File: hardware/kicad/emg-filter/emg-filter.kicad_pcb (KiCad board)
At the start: 4 copper layers, 113.7 x 234.3 mm, 78 parts, among them J1 Conn_01x02, J10 Conn_01x02, J11 Conn_01x05, J12 Conn_01x02, J13 Conn_01x02, J14 Conn_01x05, J15 Conn_01x02, J16 Conn_01x02, J17 Conn_01x05, J18 Conn_01x02, J19 Conn_01x02, J2 Conn_01x03, J20 Conn_01x05, J21 Conn_01x02, J22 Conn_01x02, J23 Conn_01x05, J24 Conn_01x02, J25 Conn_01x02, J26 Conn_01x05, J27 Conn_01x02, J28 Conn_01x02, J29 Conn_01x02, J3 Conn_02x20_Odd_Even, J30 Conn_01x02, J31 Conn_01x02, J32 Conn_01x02, J33 Conn_01x02, J34 Conn_01x02, J35 Conn_01x02, J36 Conn_01x02, J37 Conn_01x02, J38 Conn_01x02, J39 Conn_01x02, J4 Conn_01x02, J40 Conn_01x02, J41 Conn_01x02, J5 Conn_01x05, J6 Conn_01x02, J7 Conn_01x02, J8 Conn_01x05, J9 Conn_01x02, U1 LM7805_TO220, U2 LM7905_TO220, U3 ADC108S102, U4 ADC108S102

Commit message: saving progress
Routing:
- net !CS_2_PI: track 142.1 -> 135.9 mm, vias 3 -> 2
- net +3V3: track 193.7 -> 190.8 mm, vias 4 -> 3
- net SCLK_CLK_PI: track 188.6 -> 187.0 mm
- net DIN_MOSI_PI: track 191.0 -> 190.1 mm, vias 4 -> 3
- net AGND: vias 87 -> 97
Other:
- board text added: "1"
- board text added: "2"
- board text added: "3"
- board text added: "4"
- board text added: "5"
- board text added: "6"
- board text added: "7"
- board text added: "8"

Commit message: saving progress
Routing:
- net AGND: vias 97 -> 92

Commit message: gerbers
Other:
- board text added: "Prosthetic Limb EMG Motherboard Concordia University Capstone 2022 KNVBMZSFSSHS"
- board text removed: "Prosthetic Limb EMG Motherboard Concordia University Capstone 2022 VBKNMZSFSSHS"
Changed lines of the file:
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@@
     (thickness 1.6)
     (drawings 95)
-    (tracks 515)
+    (tracks 513)
     (zones 0)
     (modules 78)
@@
     (visible_elements 7FFFFFFF)
     (pcbplotparams
-      (layerselection 0x010fc_ffffffff)
+      (layerselection 0x010f0_ffffffff)
       (usegerberextensions false)
       (usegerberattributes true)
@@
       (linewidth 0.100000)
       (plotframeref false)
-      (viasonmask false)
+      (viasonmask true)
       (mode 1)
       (useauxorigin false)
@@
       (outputformat 1)
       (mirror false)
-      (drillshape 1)
+      (drillshape 0)
       (scaleselection 1)
-      (outputdirectory ""))
+      (outputdirectory "gerber/"))
   )
   (net 0 "")
@@
       (effects (font (size 0.5 0.5) (thickness 0.08)))
     )
-    (pad 1 smd roundrect (at -0.9125 0 270) (size 1.025 1.4) (layers F.Cu F.Paste F.Mask) (roundrect_rratio 0.243902)
+    (pad 1 smd roundrect (at -0.9125 0 270) (size 1.025 1.4) (layers F.Cu F.Paste F.Mask) (roundrect_rratio 0.2439014634146341)
       (net 8 "Net-(D3-Pad1)"))
-    (pad 2 smd roundrect (at 0.9125 0 270) (size 1.025 1.4) (layers F.Cu F.Paste F.Mask) (roundrect_rratio 0.243902)
+    (pad 2 smd roundrect (at 0.9125 0 270) (size 1.025 1.4) (layers F.Cu F.Paste F.Mask) (roundrect_rratio 0.2439014634146341)
       (net 5 -5V))
     (model ${KISYS3DMOD}/Resistor_SMD.3dshapes/R_0805_2012Metric.wrl
@@
       (effects (font (size 0.5 0.5) (thickness 0.08)))
     )
-    (pad 2 smd roundrect (at 0.9125 0 180) (size 1.025 1.4) (layers F.Cu F.Paste F.Mask) (roundrect_rratio 0.243902)
+    (pad 2 smd roundrect (at 0.9125 0 180) (size 1.025 1.4) (layers F.Cu F.Paste F.Mask) (roundrect_rratio 0.2439014634146341)
       (net 5 -5V))
-    (pad 1 smd roundrect (at -0.9125 0 180) (size 1.025 1.4) (layers F.Cu F.Paste F.Mask) (roundrect_rratio 0.243902)
+    (pad 1 smd roundrect (at -0.9125 0 180) (size 1.025 1.4) (layers F.Cu F.Paste F.Mask) (roundrect_rratio 0.2439014634146341)
       (net 15 "Net-(R5-Pad2)"))
     (model ${KISYS3DMOD}/Resistor_SMD.3dshapes/R_0805_2012Metric.wrl
@@
       (effects (font (size 0.5 0.5) (thickness 0.08)))
     )
-    (pad 1 smd roundrect (at -0.9125 0 180) (size 1.025 1.4) (layers F.Cu F.Paste F.Mask) (roundrect_rratio 0.243902)
+    (pad 1 smd roundrect (at -0.9125 0 180) (size 1.025 1.4) (layers F.Cu F.Paste F.Mask) (roundrect_rratio 0.2439014634146341)
       (net 2 AGND))
-    (pad 2 smd roundrect (at 0.9125 0 180) (size 1.025 1.4) (layers F.Cu F.Paste F.Mask) (roundrect_rratio 0.243902)
+    (pad 2 smd roundrect (at 0.9125 0 180) (size 1.025 1.4) (layers F.Cu F.Paste F.Mask) (roundrect_rratio 0.2439014634146341)
       (net 15 "Net-(R5-Pad2)"))
     (model ${KISYS3DMOD}/Resistor_SMD.3dshapes/R_0805_2012Metric.wrl
@@
       (effects (font (size 0.5 0.5) (thickness 0.08)))
     )
-    (pad 1 smd roundrect (at -0.9125 0 270) (size 1.025 1.4) (layers F.Cu F.Paste F.Mask) (roundrect_rratio 0.243902)
+    (pad 1 smd roundrect (at -0.9125 0 270) (size 1.025 1.4) (layers F.Cu F.Paste F.Mask) (roundrect_rratio 0.2439014634146341)
       (net 2 AGND))
-    (pad 2 smd roundrect (at 0.9125 0 270) (size 1.025 1.4) (layers F.Cu F.Paste F.Mask) (roundrect_rratio 0.243902)
+    (pad 2 smd roundrect (at 0.9125 0 270) (size 1.025 1.4) (layers F.Cu F.Paste F.Mask) (roundrect_rratio 0.2439014634146341)
       (net 4 GNDREF))
     (model ${KISYS3DMOD}/Resistor_SMD.3dshapes/R_0805_2012Metric.wrl
@@
       (effects (font (size 0.5 0.5) (thickness 0.08)))
     )
-    (pad 1 smd roundrect (at -0.9125 0 270) (size 1.025 1.4) (layers F.Cu F.Paste F.Mask) (roundrect_rratio 0.243902)
+    (pad 1 smd roundrect (at -0.9125 0 270) (size 1.025 1.4) (layers F.Cu F.Paste F.Mask) (roundrect_rratio 0.2439014634146341)
       (net 7 "Net-(D2-Pad1)"))
-    (pad 2 smd roundrect (at 0.9125 0 270) (size 1.025 1.4) (layers F.Cu F.Paste F.Mask) (roundrect_rratio 0.243902)
+    (pad 2 smd roundrect (at 0.9125 0 270) (size 1.025 1.4) (layers F.Cu F.Paste F.Mask) (roundrect_rratio 0.2439014634146341)
       (net 2 AGND))
     (model ${KISYS3DMOD}/Resistor_SMD.3dshapes/R_0805_2012Metric.wrl
@@
       (effects (font (size 0.5 0.5) (thickness 0.08)))
     )
-    (pad 1 smd roundrect (at -0.9125 0 270) (size 1.025 1.4) (layers F.Cu F.Paste F.Mask) (roundrect_rratio 0.243902)
+    (pad 1 smd roundrect (at -0.9125 0 270) (size 1.025 1.4) (layers F.Cu F.Paste F.Mask) (roundrect_rratio 0.2439014634146341)
       (net 1 +24V))
-    (pad 2 smd roundrect (at 0.9125 0 270) (size 1.025 1.4) (layers F.Cu F.Paste F.Mask) (roundrect_rratio 0.243902)
+    (pad 2 smd roundrect (at 0.9125 0 270) (size 1.025 1.4) (layers F.Cu F.Paste F.Mask) (roundrect_rratio 0.2439014634146341)
       (net 2 AGND))
     (model ${KISYS3DMOD}/Resistor_SMD.3dshapes/R_0805_2012Metric.wrl
@@
       (effects (font (size 0.5 0.5) (thickness 0.08)))
     )
-    (pad 1 smd roundrect (at -0.9125 0 90) (size 1.025 1.4) (layers F.Cu F.Paste F.Mask) (roundrect_rratio 0.243902)
+    (pad 1 smd roundrect (at -0.9125 0 90) (size 1.025 1.4) (layers F.Cu F.Paste F.Mask) (roundrect_rratio 0.2439014634146341)
       (net 3 +5V))
-    (pad 2 smd roundrect (at 0.9125 0 90) (size 1.025 1.4) (layers F.Cu F.Paste F.Mask) (roundrect_rratio 0.243902)
+    (pad 2 smd roundrect (at 0.9125 0 90) (size 1.025 1.4) (layers F.Cu F.Paste F.Mask) (roundrect_rratio 0.2439014634146341)
       (net 14 "Net-(R1-Pad2)"))
     (model ${KISYS3DMOD}/Resistor_SMD.3dshapes/R_0805_2012Metric.wrl
@@
     (effects (font (size 1 1) (thickness 0.15)))
   )
-  (gr_text "Prosthetic Limb EMG Motherboard\nConcordia University Capstone 2022\nVBKNMZSFSSHS" (at 72.39 189.23) (layer F.SilkS)
+  (gr_text "Prosthetic Limb EMG Motherboard\nConcordia University Capstone 2022\nKNVBMZSFSSHS" (at 72.39 189.23) (layer F.SilkS)
     (effects (font (size 1 1) (thickness 0.15)))
   )
@@
   (via (at 108.204 196.85) (size 0.8) (drill 0.4) (layers F.Cu B.Cu) (net 2))
   (via (at 118.364 196.85) (size 0.8) (drill 0.4) (layers F.Cu B.Cu) (net 2))
-  (segment (start 69.9008 101.0412) (end 69.2658 101.0412) (width 0.25) (layer F.Cu) (net 2))
-  (segment (start 70.243535 100.698465) (end 69.9008 101.0412) (width 0.25) (layer F.Cu) (net 2))
-  (segment (start 70.931506 100.698465) (end 70.243535 100.698465) (width 0.25) (layer F.Cu) (net 2))
+  (segment (start 69.608535 100.698465) (end 69.2658 101.0412) (width 0.25) (layer F.Cu) (net 2))
+  (segment (start 70.931506 100.698465) (end 69.608535 100.698465) (width 0.25) (layer F.Cu) (net 2))
   (segment (start 71.116041 100.883) (end 70.931506 100.698465) (width 0.25) (layer F.Cu) (net 2))
   (segment (start 72.8215 100.883) (end 71.116041 100.883) (width 0.25) (layer F.Cu) (net 2))
@@
   (segment (start 82.777049 97.028) (end 114.554 97.028) (width 0.25) (layer B.Cu) (net 6))
   (segment (start 82.742264 96.993215) (end 82.777049 97.028) (width 0.25) (layer B.Cu) (net 6))
-  (segment (start 152.908 97.028) (end 114.427 97.028) (width 0.25) (layer B.Cu) (net 6))
+  (segment (start 152.908 97.028) (end 114.554 97.028) (width 0.25) (layer B.Cu) (net 6))
   (segment (start 141.224 -12.2705) (end 141.4295 -12.2705) (width 0.25) (layer F.Cu) (net 7))
   (segment (start 141.4295 -12.2705) (end 142.24 -13.081) (width 0.25) (layer F.Cu) (net 7))
@@
   (via (at 112.014 95.504) (size 0.8) (drill 0.4) (layers F.Cu B.Cu) (net 11))
   (segment (start 112.014 199.39) (end 112.014 95.504) (width 0.25) (layer F.Cu) (net 11))
-  (segment (start 81.534 95.504) (end 151.638 95.504) (width 0.25) (layer B.Cu) (net 11))
+  (segment (start 81.534 95.504) (end 112.014 95.504) (width 0.25) (layer B.Cu) (net 11))
+  (segment (start 112.014 95.504) (end 151.638 95.504) (width 0.25) (layer B.Cu) (net 11))
   (segment (start 78.5465 100.233) (end 79.599 100.233) (width 0.25) (layer F.Cu) (net 12))
   (via (at 80.01 94.742) (size 0.8) (drill 0.4) (layers F.Cu B.Cu) (net 12))
@@
   (segment (start 148.6585 100.229) (end 149.707 100.229) (width 0.25) (layer F.Cu) (net 12))
   (via (at 150.114004 94.742) (size 0.8) (drill 0.4) (layers F.Cu B.Cu) (net 12))
-  (segment (start 110.744 94.742) (end 110.74866 94.73734) (width 0.25) (layer B.Cu) (net 12))
-  (segment (start 80.01 94.742) (end 110.744 94.742) (width 0.25) (layer B.Cu) (net 12))
-  (segment (start 110.75332 94.742) (end 110.74866 94.73734) (width 0.25) (layer B.Cu) (net 12))
-  (segment (start 150.114004 94.742) (end 110.75332 94.742) (width 0.25) (layer B.Cu) (net 12))
   (via (at 109.474 94.742) (size 0.8) (drill 0.4) (layers F.Cu B.Cu) (net 12))
   (segment (start 109.474 199.39) (end 109.474 94.742) (width 0.25) (layer F.Cu) (net 12))
+  (segment (start 109.474 94.742) (end 150.114004 94.742) (width 0.25) (layer B.Cu) (net 12))
+  (segment (start 109.474 94.742) (end 80.01 94.742) (width 0.25) (layer B.Cu) (net 12))
   (via (at 148.59 93.853) (size 0.8) (drill 0.4) (layers F.Cu B.Cu) (net 13))
   (segment (start 148.59 99.5105) (end 148.6585 99.579) (width 0.25) (layer F.Cu) (net 13))

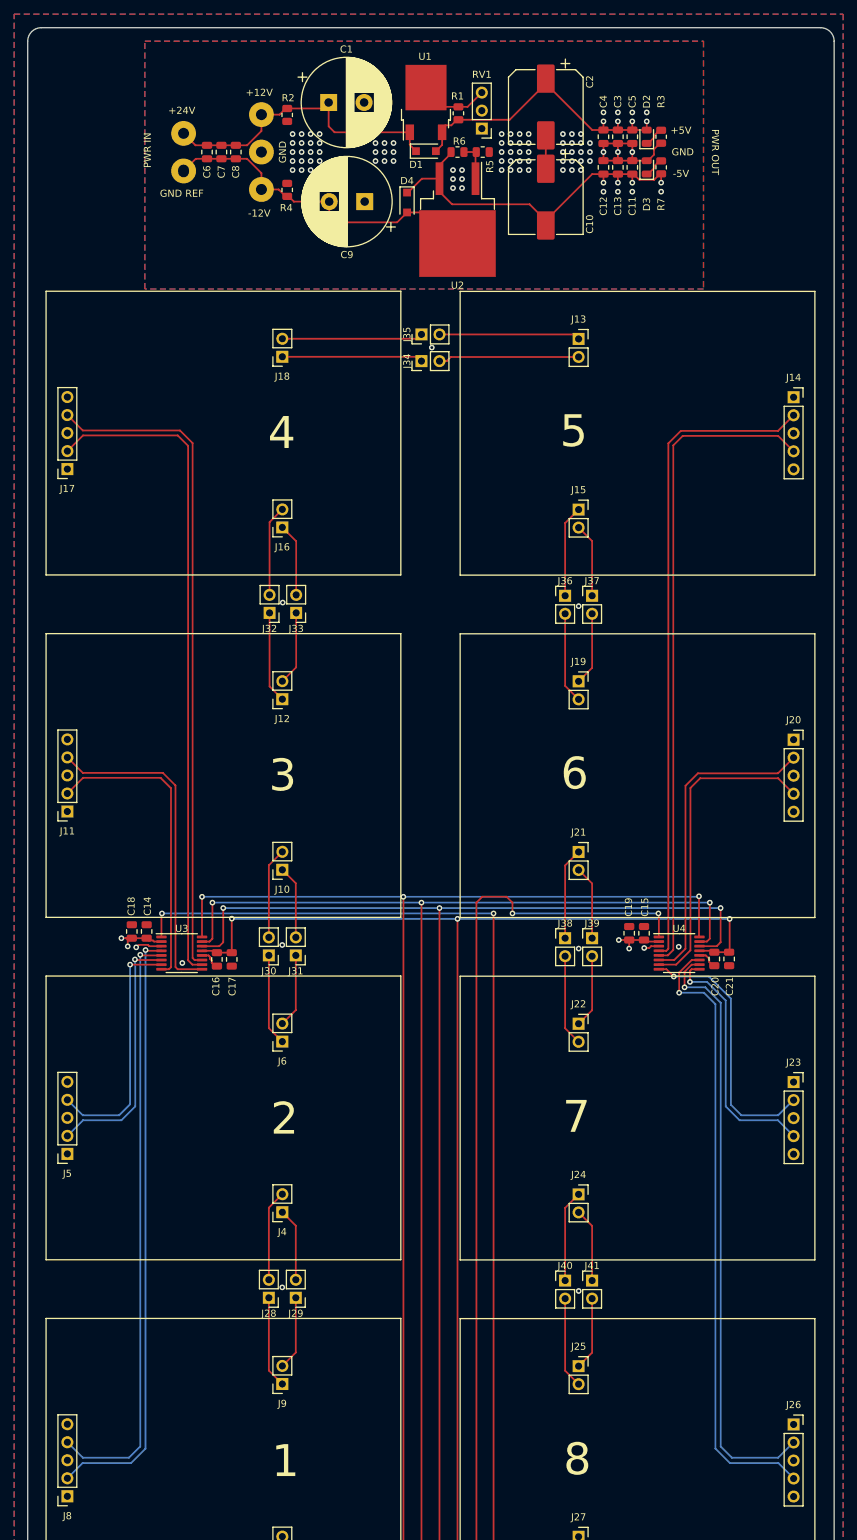
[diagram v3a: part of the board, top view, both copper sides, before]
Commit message: converted to 2 layers
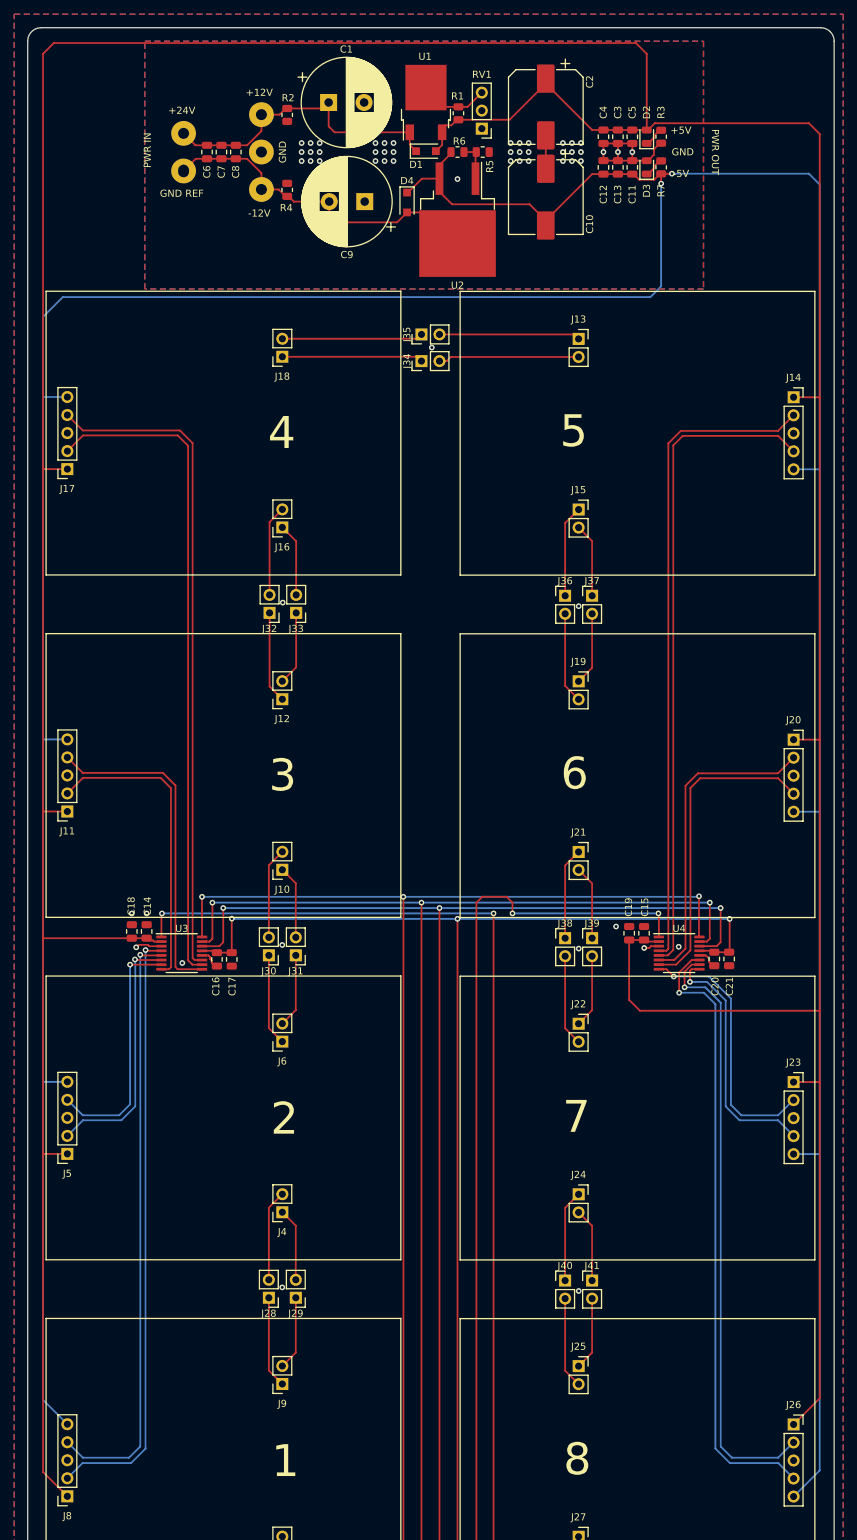
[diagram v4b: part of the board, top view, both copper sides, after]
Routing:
- net +5V: track 58.4 -> 628.7 mm, vias 12 -> 0
- net -5V: track 55.2 -> 543.5 mm, vias 8 -> 2
- net AGND: vias 92 -> 59
- removed copper zone on In1.Cu, net +5V
- removed copper zone on In2.Cu, net -5V
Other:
- copper layers 4 -> 2

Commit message: pcb mounting holes
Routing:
- net +5V: track 628.7 -> 623.5 mm
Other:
- outline, holes or cut-outs redrawn
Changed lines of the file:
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@@
   (general
     (thickness 1.6)
-    (drawings 95)
+    (drawings 99)
     (tracks 515)
     (zones 0)
@@
       (linewidth 0.100000)
       (plotframeref false)
-      (viasonmask true)
+      (viasonmask false)
       (mode 1)
       (useauxorigin false)
@@
     )
   )
+  (gr_circle (center 58.41124 191.135) (end 59.91124 191.135) (layer Edge.Cuts) (width 0.15))
+  (gr_circle (center 58.41124 -24.135) (end 59.91124 -24.135) (layer Edge.Cuts) (width 0.15))
+  (gr_circle (center 163.195 -24.135) (end 164.695 -24.135) (layer Edge.Cuts) (width 0.15))
+  (gr_circle (center 163.195 191.135) (end 164.695 191.135) (layer Edge.Cuts) (width 0.15))
   (gr_text 5 (at 130.937 28.321) (layer F.SilkS)
     (effects (font (size 4.5 4.5) (thickness 0.5)))
@@
     (effects (font (size 1 1) (thickness 0.15)))
   )
-  (gr_text "Prosthetic Limb EMG Motherboard\nConcordia University Capstone 2022\nKNVBMZSFSSHS" (at 72.39 189.23) (layer F.SilkS)
+  (gr_text "Prosthetic Limb EMG Motherboard\nConcordia University Capstone 2022\nKNVBMZSFSSHS" (at 76.2 3.175) (layer F.SilkS)
     (effects (font (size 1 1) (thickness 0.15)))
   )
@@
   (segment (start 141.3995 -14.1455) (end 142.367 -15.113) (width 0.25) (layer F.Cu) (net 3))
   (segment (start 141.224 -14.1455) (end 141.3995 -14.1455) (width 0.25) (layer F.Cu) (net 3))
-  (segment (start 141.224 -14.1455) (end 141.224 -24.892) (width 0.25) (layer F.Cu) (net 3))
+  (segment (start 56.134 -16.002) (end 56.134 33.528) (width 0.25) (layer F.Cu) (net 3))
+  (segment (start 66.548 -26.416) (end 56.134 -16.002) (width 0.25) (layer F.Cu) (net 3))
+  (segment (start 139.7 -26.416) (end 66.548 -26.416) (width 0.25) (layer F.Cu) (net 3))
   (segment (start 141.224 -24.892) (end 139.7 -26.416) (width 0.25) (layer F.Cu) (net 3))
-  (segment (start 139.7 -26.416) (end 57.658 -26.416) (width 0.25) (layer F.Cu) (net 3))
-  (segment (start 57.658 -26.416) (end 56.134 -24.892) (width 0.25) (layer F.Cu) (net 3))
-  (segment (start 56.134 -24.892) (end 56.134 33.528) (width 0.25) (layer F.Cu) (net 3))
+  (segment (start 141.224 -14.1455) (end 141.224 -24.892) (width 0.25) (layer F.Cu) (net 3))
   (segment (start 77.663 -10.099) (end 75.946 -8.382) (width 0.25) (layer F.Cu) (net 4))
   (segment (start 79.248 -10.099) (end 77.663 -10.099) (width 0.25) (layer F.Cu) (net 4))

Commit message: gerbers
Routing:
- net -5V: track 543.5 -> 544.2 mm
